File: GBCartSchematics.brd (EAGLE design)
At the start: 65.7 x 80 mm, 5 parts

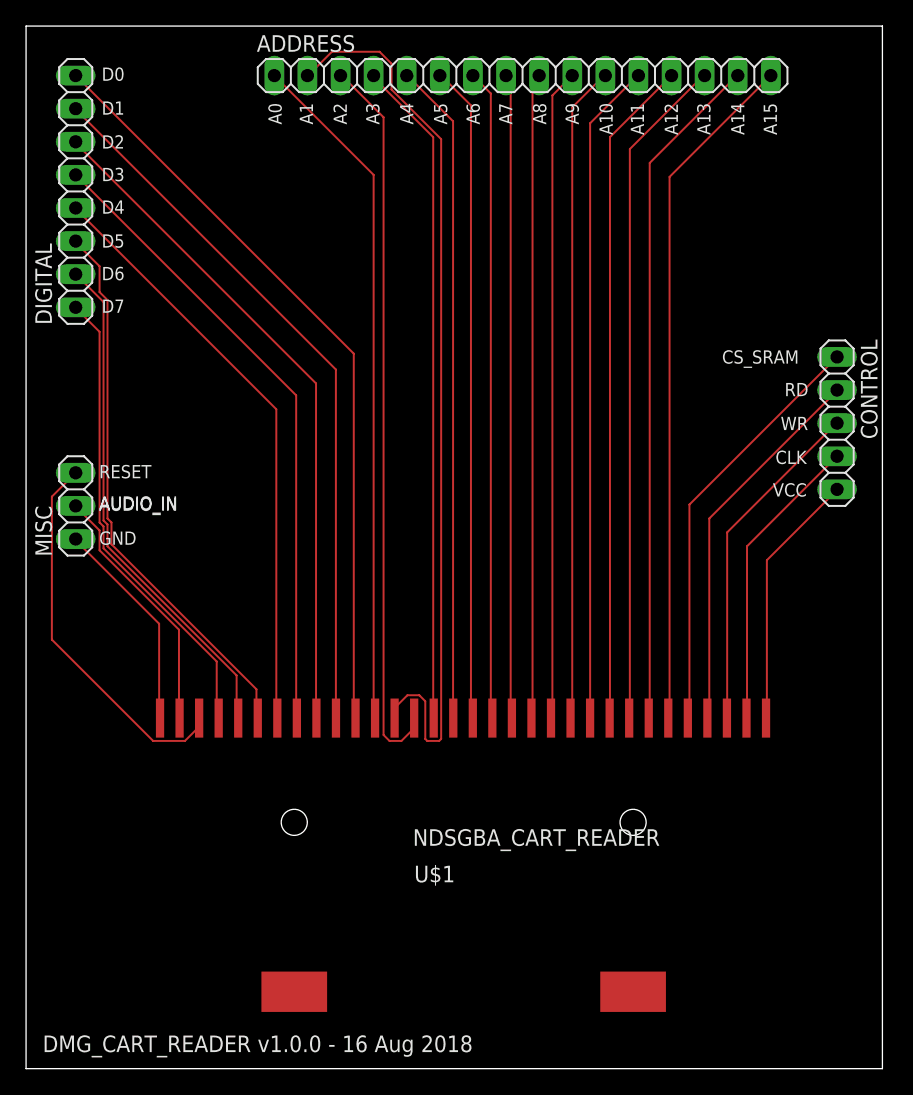
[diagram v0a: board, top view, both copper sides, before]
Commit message: Improved wiring (omg, lol) and added gitignore, fixed text issues on addressing pins
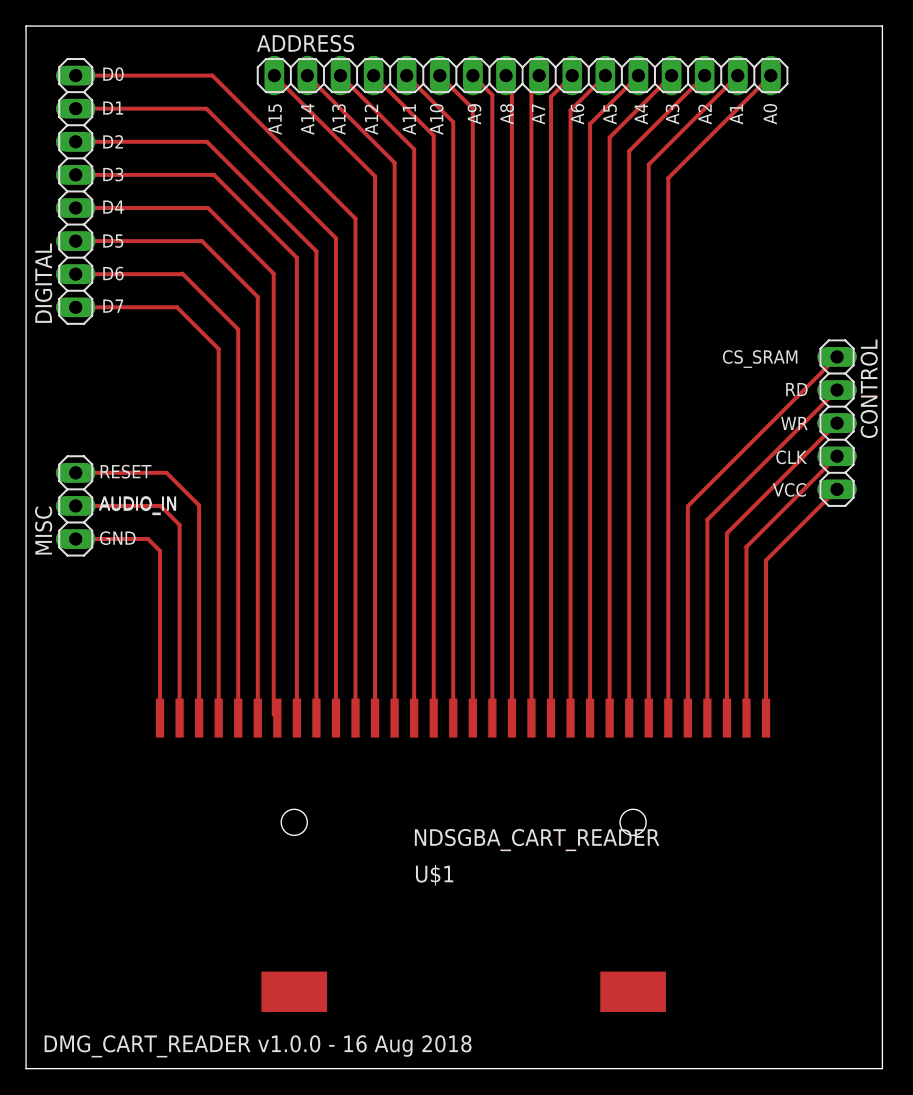
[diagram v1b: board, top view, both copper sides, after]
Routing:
- net A14: track 68.9 -> 52.1 mm
- net D3: track 48.7 -> 54.9 mm
- net D0: track 58.2 -> 64.3 mm
- net D4: track 45.5 -> 51.5 mm
- net D2: track 51.9 -> 57.8 mm
- net D1: track 55.0 -> 60.9 mm
- net D5: track 42.4 -> 48.1 mm
- net D6: track 39.2 -> 44.1 mm
- net D7: track 36.1 -> 40.6 mm
- net A13: track 55.7 -> 51.6 mm
- net AUDIO_IN: track 19.6 -> 23.4 mm
- net GND: track 16.4 -> 19.7 mm
- net RESET: track 29.2 -> 26.8 mm
